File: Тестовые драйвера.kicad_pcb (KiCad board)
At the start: 4 copper layers, 72.7 x 84.6 mm, 107 parts, among them J1 Conn_01x01, J2 Conn_01x01, J3 Conn_01x01, J4 Conn_01x01, J5 Conn_01x01, Q1 C2M0280120D, Q2 C2M0280120D, Q3 C2M0280120D, Q4 C2M0280120D, Q5 C2M0280120D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

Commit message: Определились с ТЗ
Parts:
- moved C12 83.3 mm to (214.0, 27.5)
- moved D4 83.3 mm to (214.5, 25.0)
- moved D10 66.4 mm to (180.2, 31.5)
- moved D2 66.4 mm to (191.0, 31.5)
- moved D3 66.4 mm to (200.2, 29.8)
- moved R6 66.4 mm to (201.2, 33.8)
- moved C2 40.9 mm to (176.5, 123.5)
- moved C3 40.9 mm to (179.0, 123.5)
- moved C7 40.9 mm to (161.5, 126.0)
- moved C8 40.9 mm to (159.0, 126.0)
- moved D1 40.9 mm to (169.0, 122.5)
- moved J6 39.8 mm to (96.6, 163.0)
- moved D17 35.6 mm to (68.5, 144.0)
- moved C11 24.0 mm to (139.0, 138.0)
- moved C16 24.0 mm to (159.0, 130.0)
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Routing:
- net ClampH: track 84.6 -> 0.80 mm, vias 2 -> 0
- net Net-(D1-DESAT): track 69.0 -> 0.00 mm, vias 1 -> 0
- net -4VH: track 18.5 -> 0.00 mm
- net +15VH: track 17.2 -> 0.00 mm
- net OUT: track 14.0 -> 0.00 mm
- net OutL1: track 1.19 -> 0.00 mm, vias 7 -> 0
- removed copper zone on F.Cu, net OutH1
- removed copper zone on B.Cu, net OutL1
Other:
- board size 72.7 x 84.6 mm -> 146.2 x 68 mm

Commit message: VER1.0: разделил плату драйвера и силовую
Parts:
- added J7: Conn_01x04, Connector_PinSocket_2.54mm:PinSocket_1x04_P2.54mm_Vertical, B.Cu at (286.0, 285.9)
- J4, J5: value Conn_01x01 -> Conn_01x04; footprint Connector_My:Power_Wire -> Connector_PinSocket_2.54mm:PinSocket_1x04_P2.54mm_Vertical
- R14, R19, R33, R38, R4, R46: value Rdesat -> 10k
- moved C18 339.1 mm to (400.0, 356.6)
- moved C19 339.1 mm to (400.0, 360.0)
- moved C39 339.1 mm to (392.2, 385.2)
- moved C46 339.1 mm to (523.2, 367.7)
- moved D11 339.1 mm to (543.7, 325.1)
- moved D6 339.1 mm to (531.7, 247.9)
- moved J6 339.1 mm to (369.3, 364.6)
- moved C11 339.1 mm to (411.7, 339.6)
- moved C12 339.1 mm to (486.7, 229.1)
- moved C16 339.1 mm to (431.7, 331.6)
- moved C17 339.1 mm to (429.2, 331.6)
- moved C2 339.1 mm to (449.2, 325.1)
- moved C23 339.1 mm to (533.4, 335.2)
- moved C28 339.1 mm to (408.3, 373.8)
- moved C29 339.1 mm to (408.3, 378.1)
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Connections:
- J4 pad 1: GND1 -> unconnected-(J4-Pin_1-Pad1)
- J5 pad 1: +12V -> unconnected-(J5-Pin_1-Pad1)
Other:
- board size 146.2 x 68 mm -> 114.4 x 54.6 mm

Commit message: VER1.0: поработал над шинами
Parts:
- added J10: Conn_01x01, Bush_my:Bush_5x3, F.Cu at (351.8, 312.0)
- added J11: Conn_01x01, Bush_my:Bush_5x3, F.Cu at (351.8, 295.0)
- added J12: Conn_01x01, Bush_my:Bush_5x3, F.Cu at (354.5, 305.0)
- added J13: Conn_01x01, Bush_my:Bush_5x3, F.Cu at (354.5, 288.0)
- added J14: Conn_01x03, Bush_my:247_border_my, F.Cu at (303.2, 306.8)
- added J15: Conn_01x03, Bush_my:247_border_my, F.Cu at (303.2, 272.8)
- added J16: Conn_01x03, Bush_my:247_border_my, F.Cu at (303.2, 289.8)
- added J8: Conn_01x01, Bush_my:Bush_5x3, F.Cu at (348.0, 268.2)
- added J9: Conn_01x01, Bush_my:Bush_5x3, F.Cu at (348.0, 302.2)
- J1, J2, J3: footprint Bush_my:Bush_SMD_M3 -> Bush_my:Bush_5x3
- moved D8 265.5 mm to (285.5, 267.2), turned to 180 degrees
- moved D9 263.3 mm to (283.0, 271.5), turned to 90 degrees
- moved D11 254.9 mm to (295.5, 267.2), turned to 180 degrees
- moved R21 161.6 mm to (286.2, 275.0)
- moved D17 35.8 mm to (306.8, 355.2), turned to 90 degrees
- moved J1 21.9 mm to (348.0, 285.2), turned to -90 degrees
- moved J2 11.8 mm to (351.8, 278.0)
- moved J5 10.0 mm to (317.8, 285.9)
- moved J7 10.0 mm to (276.0, 285.9)
- moved C24 4.60 mm to (284.5, 281.2)
- moved C25 4.60 mm to (287.0, 281.2)
- moved C30 4.60 mm to (294.2, 298.0)
- moved C31 4.60 mm to (294.2, 300.2)
- moved C32 4.60 mm to (297.0, 281.2)
- moved C35 4.60 mm to (289.5, 281.2)
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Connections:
- C24 pad 1: GNDPWR -> Drain_Low
- C25 pad 1: GNDPWR -> Drain_Low
- C32 pad 1: GNDPWR -> Drain_Low
- C35 pad 2: GNDPWR -> Drain_Low
- C36 pad 2: GNDPWR -> Drain_Low
- C37 pad 2: GNDPWR -> Drain_Low
- C41 pad 2: GNDPWR -> Drain_Low
- C43 pad 2: GNDPWR -> Drain_Low
- D17 pad 6: GNDPWR -> Drain_Low
- D5 pad 2: GNDPWR -> Drain_Low
- D7 pad 3: GNDPWR -> Drain_Low
- J1 pad 1: GNDPWR -> Drain_Low
- Q4 pad 3: GNDPWR -> Drain_Low
- Q5 pad 3: GNDPWR -> Drain_Low
- Q6 pad 3: GNDPWR -> Drain_Low
- R33 pad 1: GNDPWR -> Drain_Low
- R38 pad 1: GNDPWR -> Drain_Low
- R46 pad 1: GNDPWR -> Drain_Low
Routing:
- added copper zone on B.Cu, net Drain_Low
- added copper zone on F.Cu, net Drain_Low
- added copper zone on B.Cu, net OUT
- added copper zone on F.Cu, net OUT
- added copper zone on B.Cu, net VDC
- added copper zone on F.Cu, net VDC
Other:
- copper layers 4 -> 2

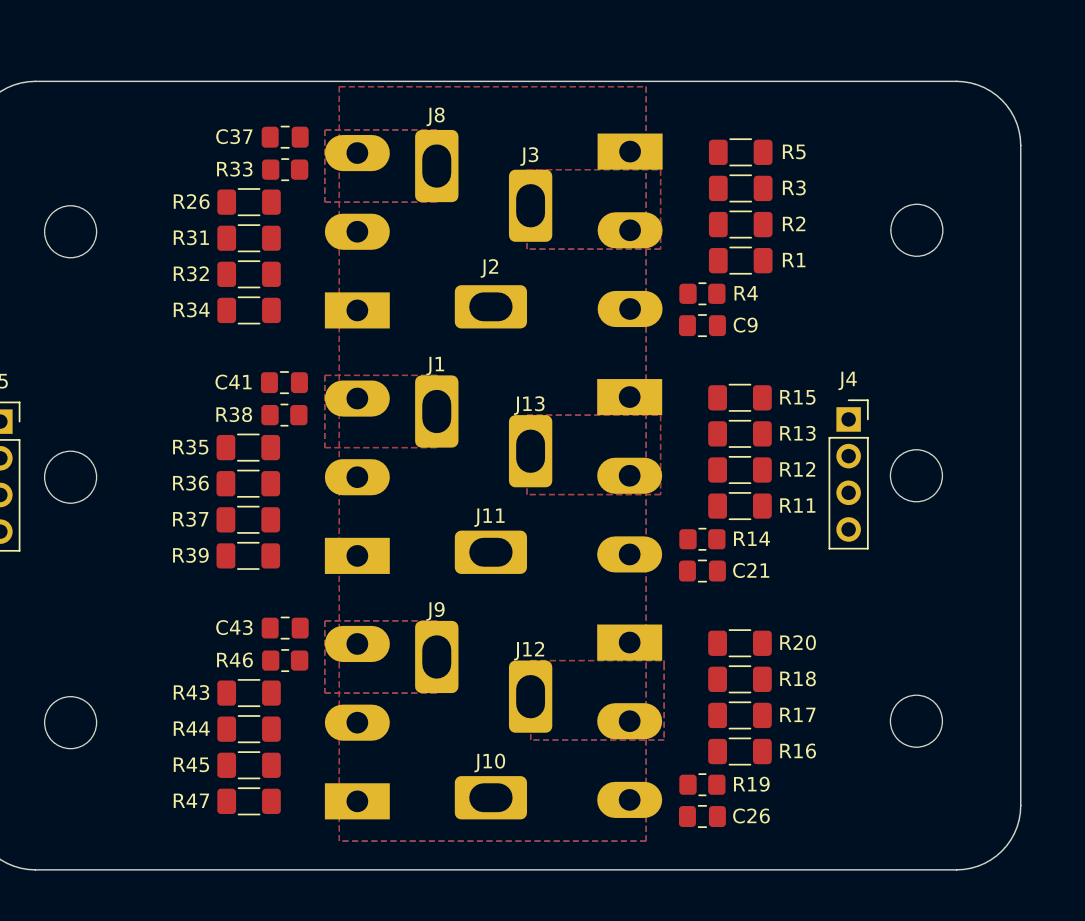
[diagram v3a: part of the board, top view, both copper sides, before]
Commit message: VER1.0.1: убрал вводы шин наружу от ножек транзисторов
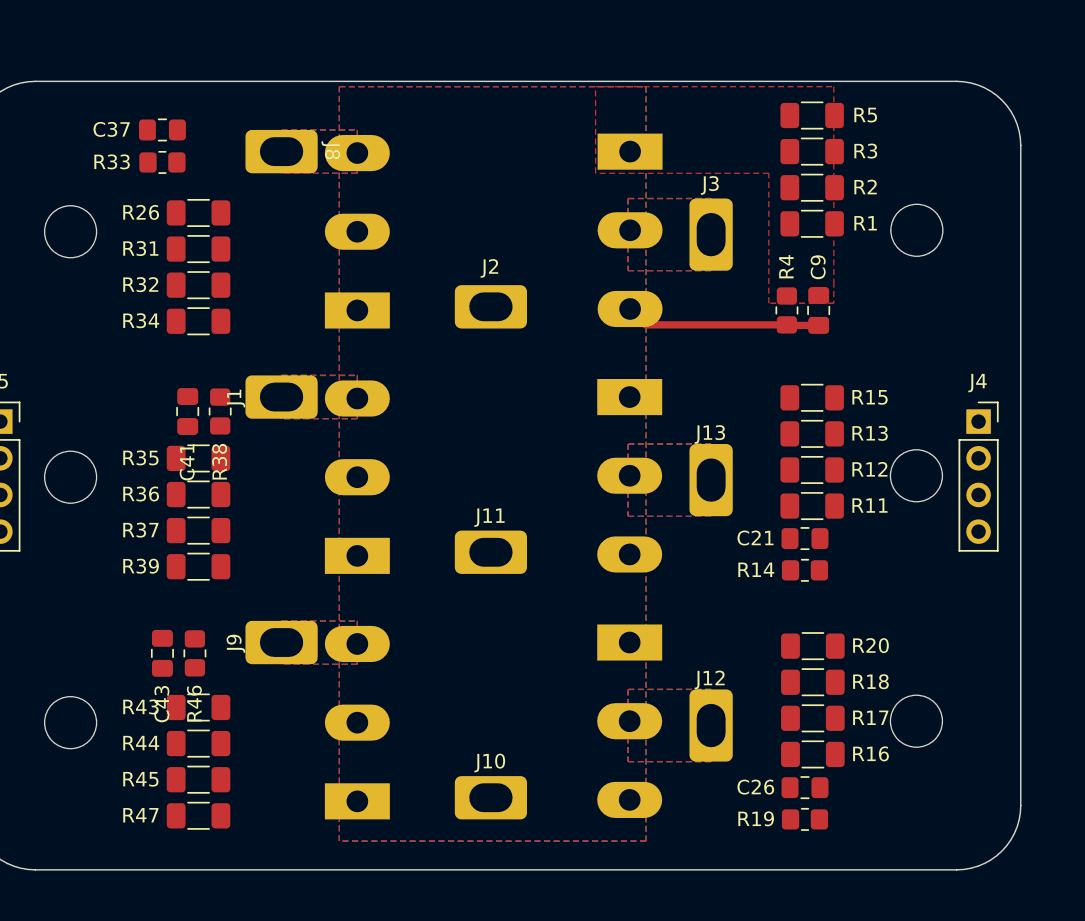
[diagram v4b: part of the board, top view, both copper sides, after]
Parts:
- moved J12 12.7 mm to (367.0, 307.0), turned to -90 degrees
- moved J13 12.7 mm to (367.0, 290.0)
- moved J3 12.7 mm to (367.0, 273.0)
- moved J1 10.8 mm to (337.2, 284.2), turned to 0 degrees
- moved J8 10.8 mm to (337.2, 267.2), turned to 0 degrees
- moved J9 10.8 mm to (337.2, 301.2), turned to 180 degrees
- moved J4 9.00 mm to (385.5, 285.9)
- moved C43 8.68 mm to (329.0, 302.0), turned to 90 degrees
- moved C37 8.51 mm to (329.0, 265.8)
- moved R33 8.51 mm to (329.0, 268.0)
- moved C9 8.12 mm to (374.4, 278.2), turned to -90 degrees
- moved R19 7.49 mm to (373.5, 313.5), turned to 180 degrees
- moved C21 7.45 mm to (373.5, 294.1), turned to 0 degrees
- moved R14 7.42 mm to (373.5, 296.2), turned to 180 degrees
- moved C26 7.38 mm to (373.5, 311.3), turned to 0 degrees
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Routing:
- net OUT: track 0.00 -> 13.5 mm
- net ClampH: track 0.80 -> 0.07 mm
- added copper zone on F.Cu, net ClampH
